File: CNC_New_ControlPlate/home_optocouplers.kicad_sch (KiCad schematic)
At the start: 17 parts, among them U1 PC847

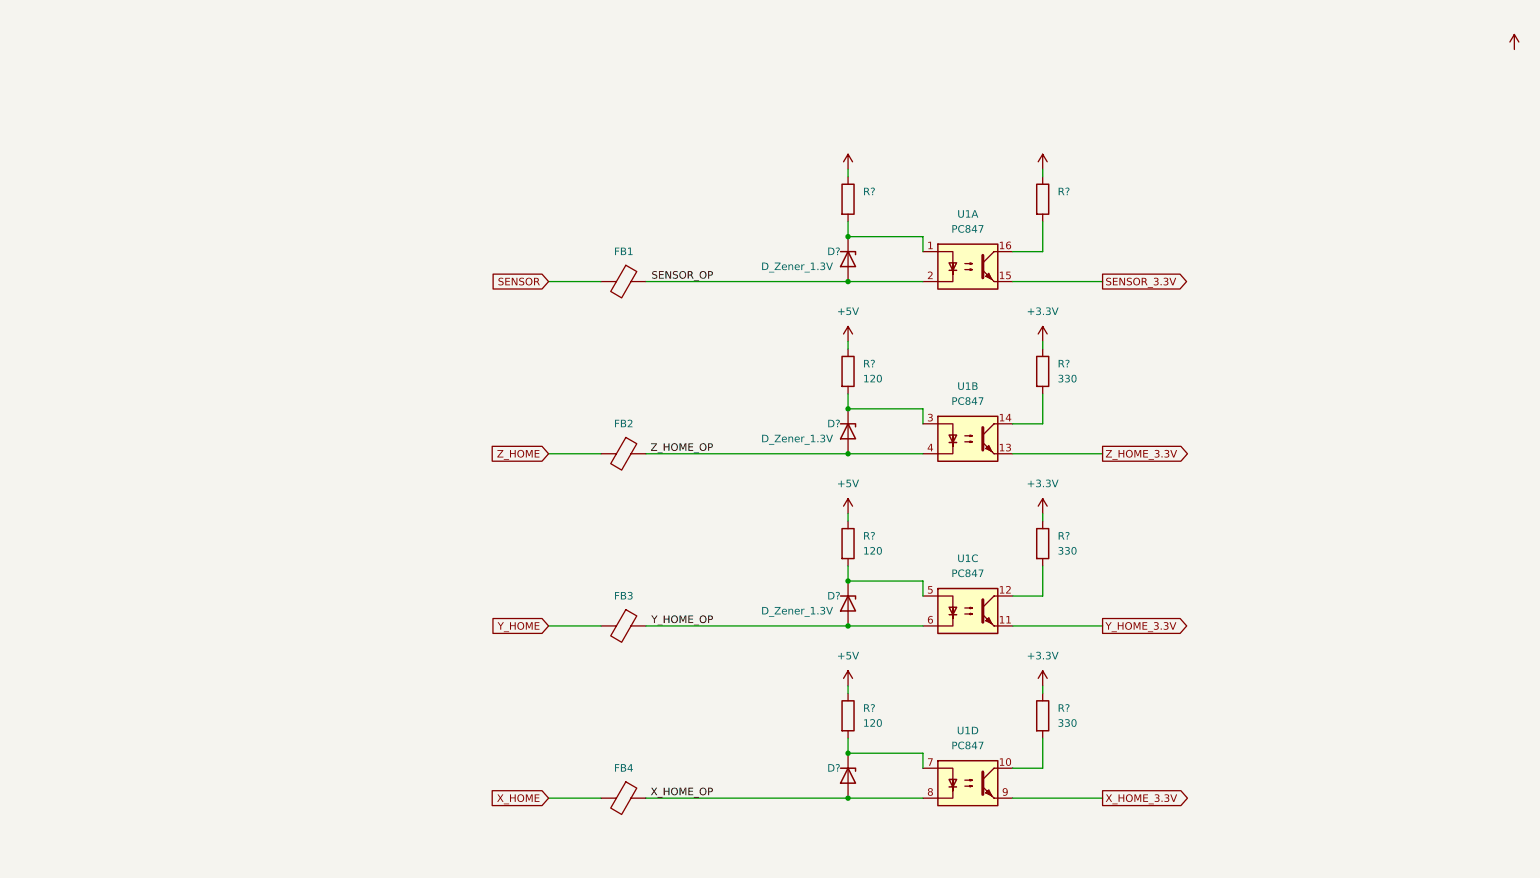
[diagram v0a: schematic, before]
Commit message: Датчики и щуп через оптопары
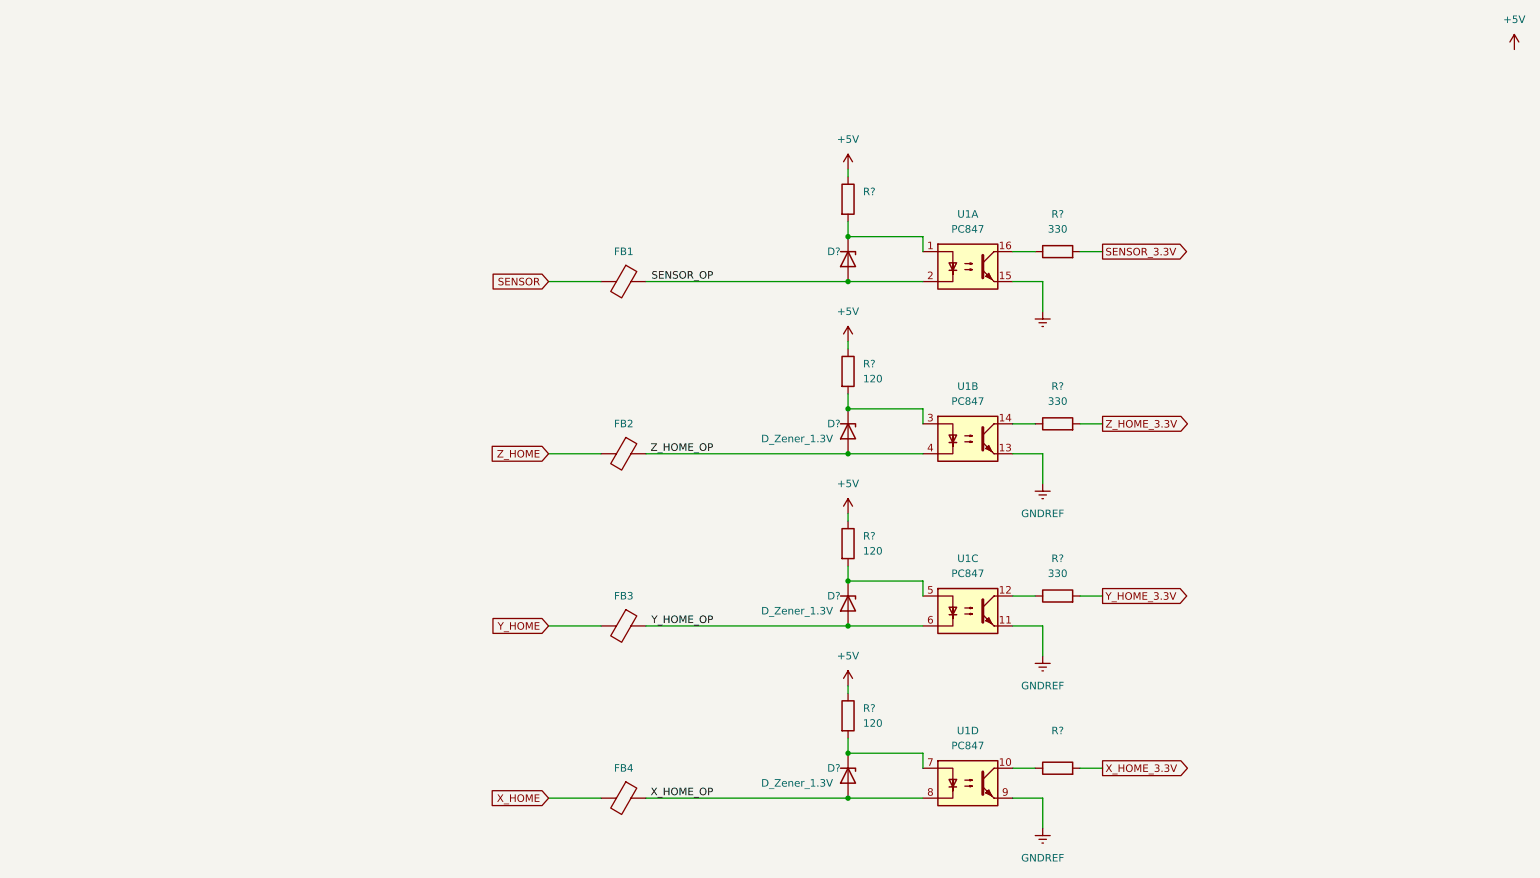
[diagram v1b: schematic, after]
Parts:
- removed R?: (no value), symbol Device:R
- removed R? (x3): 120, Diode_SMD:D_0603_1608Metric, symbol Device:R
- removed R? (x3): 330, Diode_SMD:D_0603_1608Metric, symbol Device:R
- added R? (x3): 120, Resistor_SMD:R_0603_1608Metric, symbol Device:R
- added R? (x3): 330, Resistor_SMD:R_0603_1608Metric, symbol Device:R
- added R?: (no value), symbol Device:R
- D?: value D_Zener_1.3V -> (none); footprint Diode_SMD:D_0603_1608Metric -> (none)
- D?: value (none) -> D_Zener_1.3V; footprint (none) -> Diode_SMD:D_0603_1608Metric
- FB2, FB3, FB4: value (none) -> FerriteBead; footprint (none) -> Resistor_SMD:R_0603_1608Metric
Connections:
- net +5V: now also R?.1, R?.1, R?.1
- net SENSOR_3.3V: now also R?.2; no longer U1.15
- net X_HOME_3.3V: now also R?.2; no longer U1.9
- net Y_HOME_3.3V: now also R?.2; no longer U1.11
- net Z_HOME_3.3V: now also R?.2; no longer U1.13
- net at U1.16: now also R?.1
- net at D?.1 (K), U1.5: now also R?.2
- net at D?.1 (K), U1.3: now also R?.2
- net at D?.1 (K), U1.7: now also R?.2
- net at U1.14: now also R?.1
- net at U1.10: now also R?.1
- net at U1.12: now also R?.1
- new net GNDREF: U1.11, U1.13, U1.15, U1.9

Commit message: Обновил датчики HOME
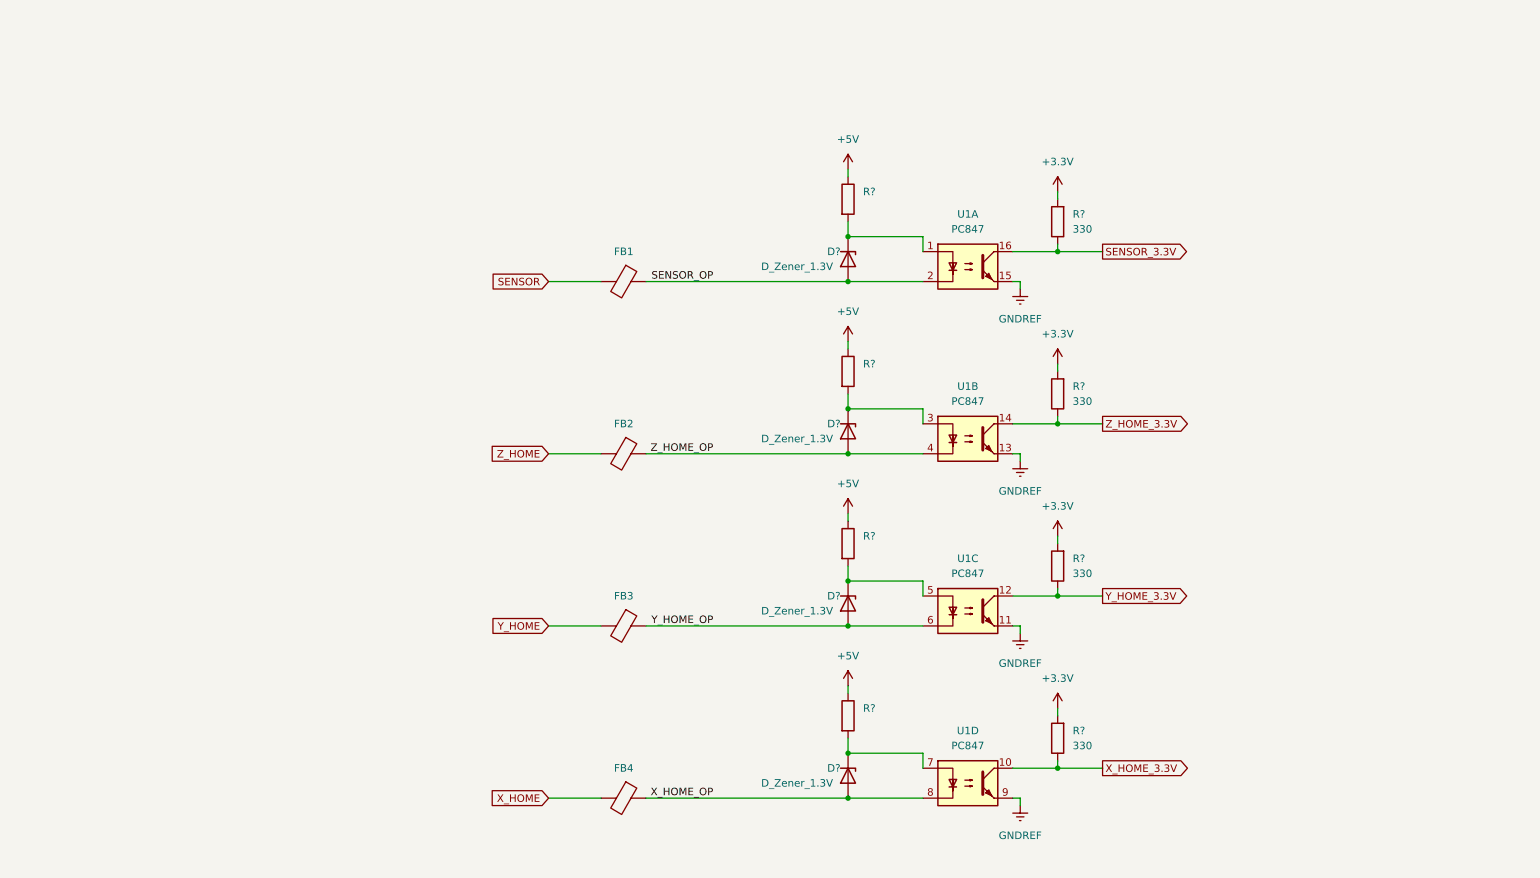
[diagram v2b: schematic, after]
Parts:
- removed R? (x2): 330, Resistor_SMD:R_0603_1608Metric, symbol Device:R
- removed R?: (no value), symbol Device:R
- added R? (x3): 330, Resistor_SMD:R_0603_1608Metric, symbol Device:R
- D?: value (none) -> D_Zener_1.3V; footprint (none) -> Diode_SMD:D_0603_1608Metric
- FB1: value (none) -> FerriteBead; footprint (none) -> Resistor_SMD:R_0603_1608Metric
- R? (x3): value 120 -> (none)
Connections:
- net SENSOR_3.3V: now also R?.1, U1.16; no longer R?.2
- net X_HOME_3.3V: now also U1.10, R?.1
- net Y_HOME_3.3V: now also U1.12, R?.1
- net Z_HOME_3.3V: now also U1.14, R?.1
- new net +3V3: R?.2, R?.2, R?.2, R?.2
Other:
- moved on the sheet: R?

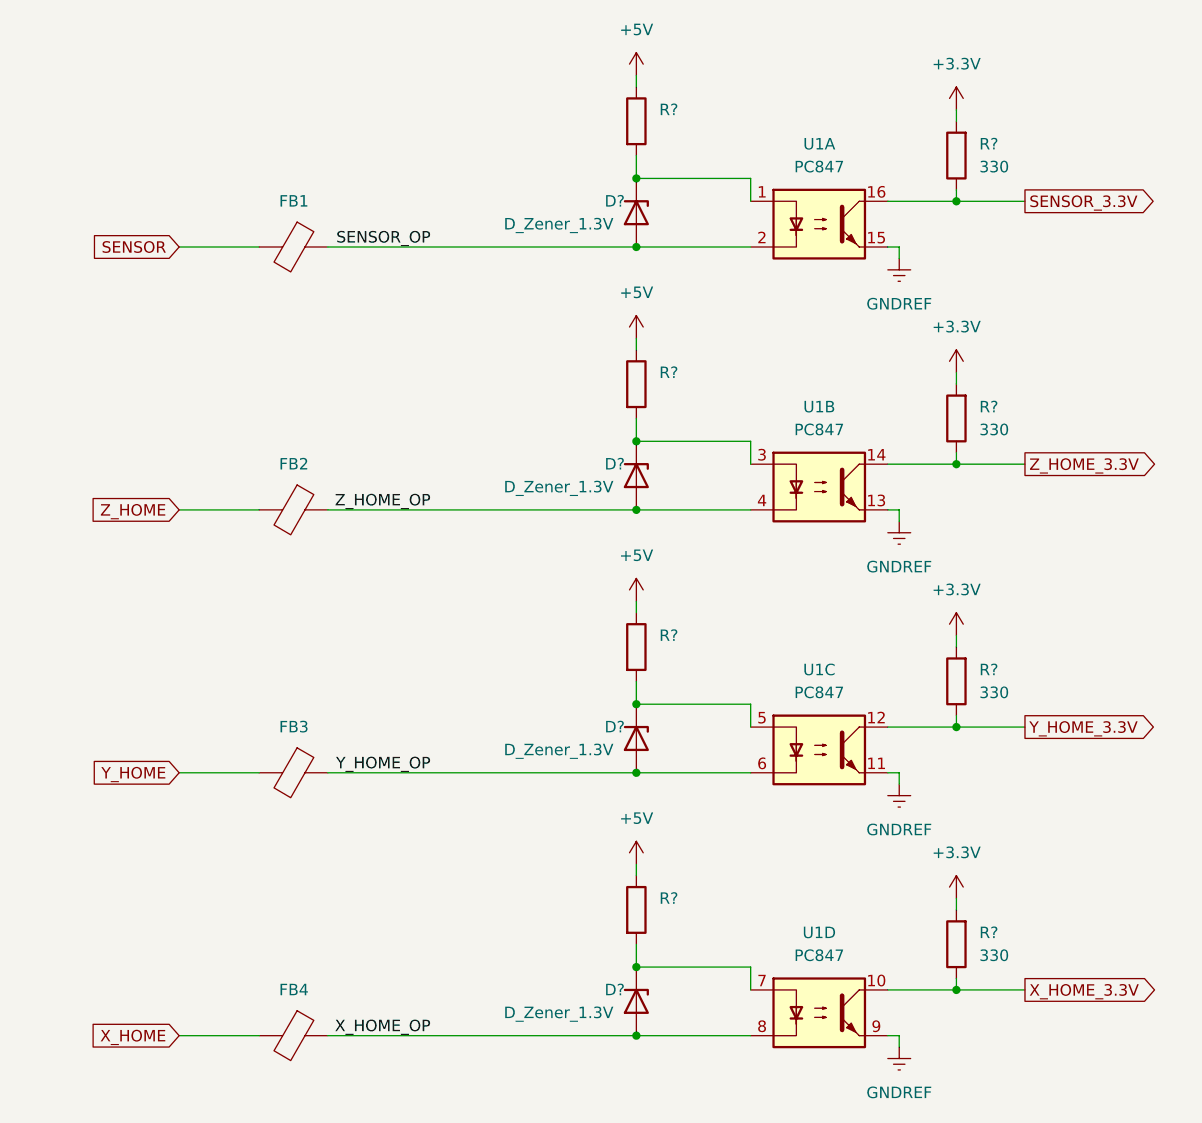
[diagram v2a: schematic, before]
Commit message: [+] Лист STEPPERS [+] Разъем подключения шаговиков [+] Моделька драйвера дифф линий [+] Управление X Y заведено через драйверы дифф линий [+] Управление Z заведено через инвертор [+] Enable Z заведен через инвертор к Disable Steppers
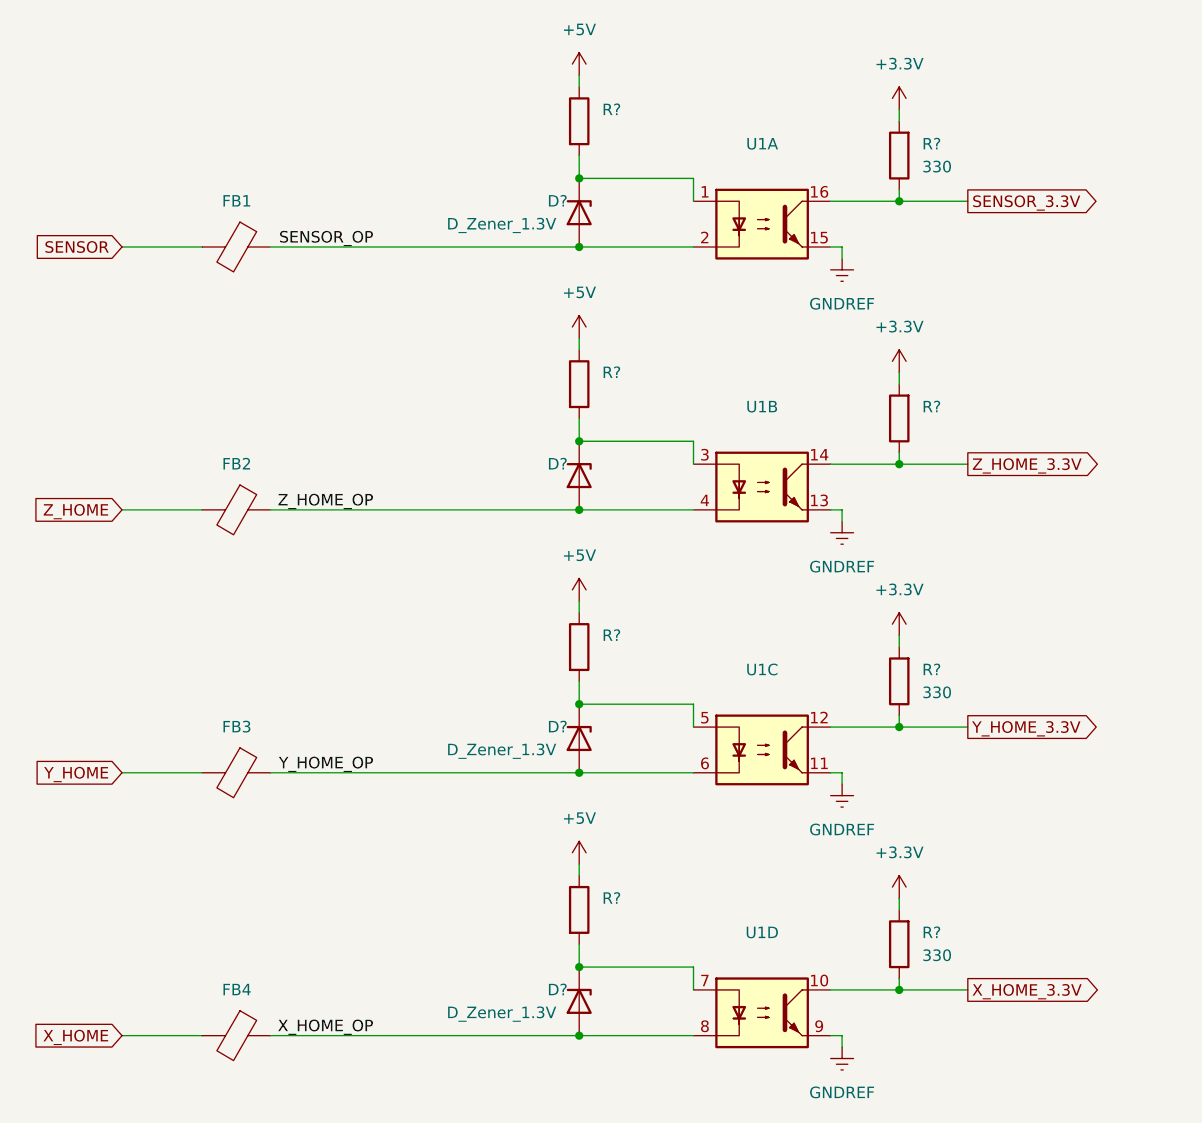
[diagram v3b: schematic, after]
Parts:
- D?: value D_Zener_1.3V -> (none); footprint Diode_SMD:D_0603_1608Metric -> (none)
- FB2: value FerriteBead -> (none); footprint Resistor_SMD:R_0603_1608Metric -> (none)
- R?: footprint Resistor_SMD:R_0603_1608Metric -> (none)
- R?: value 330 -> (none); footprint Resistor_SMD:R_0603_1608Metric -> (none)
- U1: value PC847 -> (none); footprint Package_DIP:DIP-16_W7.62mm -> (none)
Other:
- moved on the sheet: D?, FB1, FB2, FB3, FB4, R?, U1A, U1B, U1C, U1D
